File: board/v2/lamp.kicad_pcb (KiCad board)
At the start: 4 copper layers, 28 x 28 mm, 41 parts, among them J1 Conn_01x01_Female, J2 Conn_01x01_Female, J3 Conn_01x01_Female, J4 Conn_01x01_Female, J5 Conn_01x01_Female, J6 Conn_01x01_Female, J7 Conn_01x01_Female, J8 Conn_ARM_JTAG_SWD_10, U1 STM32G071GxU, U2 TLV2333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

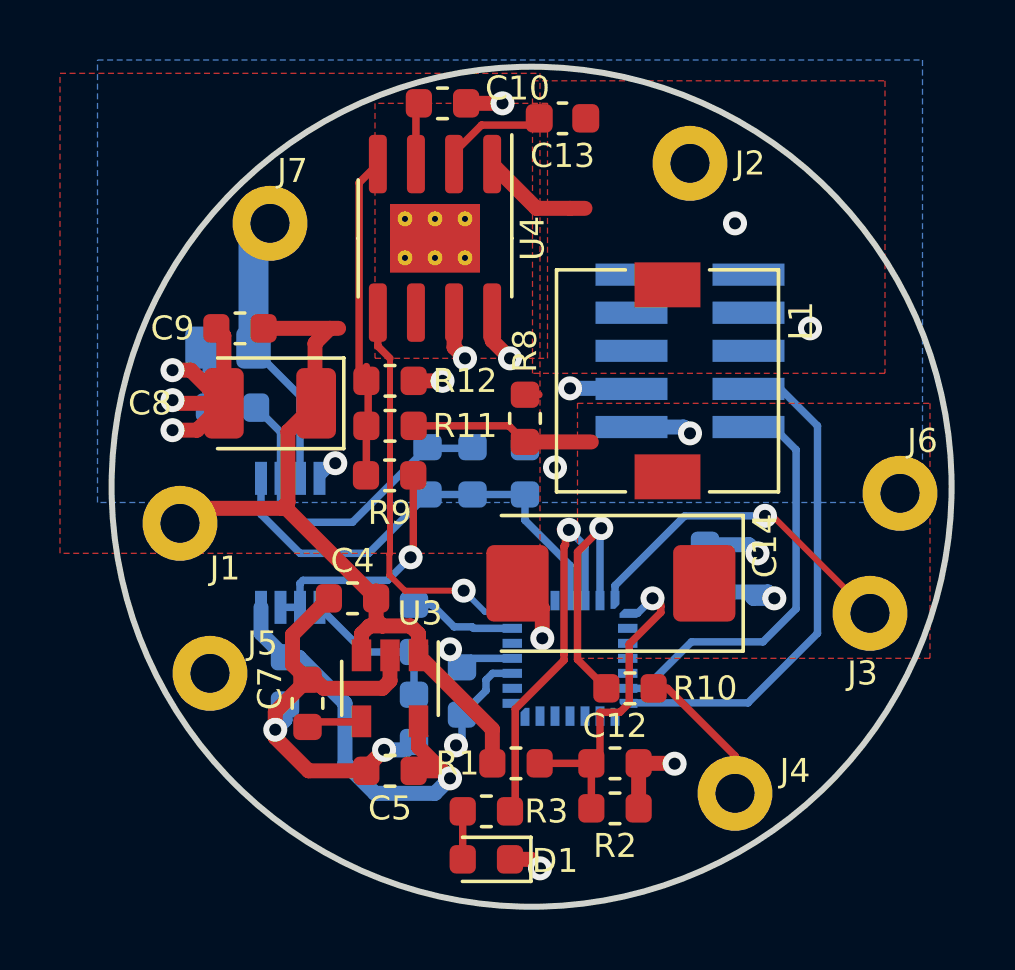
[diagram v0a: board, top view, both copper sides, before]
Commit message: hardware: Add reverse polarity protection
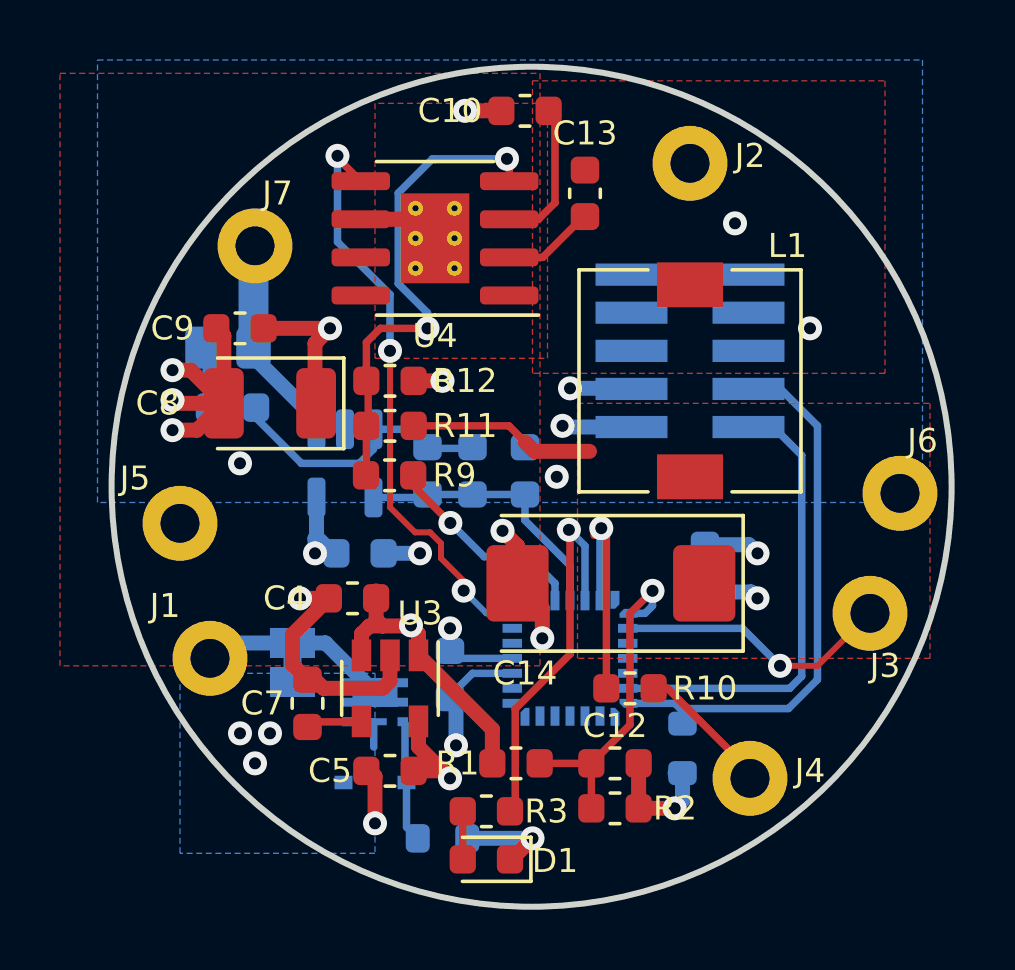
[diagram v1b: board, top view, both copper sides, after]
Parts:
- removed C3: 100n, Capacitor_SMD:C_0603_1608Metric
- removed R8: 100k, Resistor_SMD:R_0603_1608Metric
- added D2: D_Zener, Diode_SMD:D_SOD-323, B.Cu at (130.5, 93.6)
- added JP1: Jumper_2_Bridged, Jumper:SolderJumper-2_P1.3mm_Bridged_Pad1.0x1.5mm, B.Cu at (127.8, 89.6)
- added Q1: SiA453EDJ, Package_TO_SOT_SMD:Vishay_PowerPAK_SC70-6L_Single, B.Cu at (130.5, 91.0)
- added R7: R, Resistor_SMD:R_0603_1608Metric, B.Cu at (132.8, 95.5)
- R1: value 47k -> 680k
- R11: value 8.2k -> 100k
- R12: value 2.2k -> 47k
- R2, R9: value 10k -> 220k
- R4: value 10k -> 470k
- U2: value TLV2333 -> TLV333; footprint Package_SO:TSSOP-8_3x3mm_P0.65mm -> Package_TO_SOT_SMD:SOT-23-5
- moved R4 9.80 mm to (140.8, 92.5)
- moved J5 5.10 mm to (124.0, 85.0)
- moved C11 4.93 mm to (130.0, 86.0), turned to 0 degrees
- moved J1 4.61 mm to (125.0, 89.5)
- moved U2 3.22 mm to (129.5, 83.0)
- moved C10 2.76 mm to (135.5, 71.2), turned to 180 degrees
- moved C13 2.61 mm to (137.5, 74.0), turned to 90 degrees
- moved J7 0.90 mm to (126.5, 75.8)
- moved L1 0.75 mm to (141.0, 80.2)
- moved J4 0.71 mm to (143.0, 93.5)
- moved C2 0.68 mm to (133.0, 90.0)
- turned U4 to 180 degrees
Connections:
- C4 pad 1: /VIN -> /Vin
- C8 pad 1: /VIN -> /Vin
- C9 pad 1: /VIN -> /Vin
- J1 pad 1: /VIN -> /Vbat
- R1 pad 2: /VIN -> /Vin
- R4 pad 1: /SETPOINT -> GND
- R4 pad 2: /SETPOINT_PWM -> /SWDCLK
- R9 pad 2: Net-(R9-Pad2) -> /SETPOINT
- U1 pad 10: unconnected-(U1-Pad10) -> /SETPOINT
- U1 pad 14: /BTN -> unconnected-(U1-Pad14)
- U1 pad 16: unconnected-(U1-Pad16) -> /BTN
- U1 pad 6: /SETPOINT_PWM -> unconnected-(U1-Pad6)
- U2 pad 1: /ISENSE_BUFD -> /ISENSE
- U2 pad 2: Net-(C6-Pad1) -> GND
- U2 pad 3: /ISENSE -> Net-(C6-Pad1)
- U2 pad 4: GND -> /ISENSE_BUFD
- U2 pad 5: /SETPOINT -> +3V3
- U3 pad 1: /VIN -> /Vin
- U3 pad 3: /VIN -> /Vin
- U4 pad 6: unconnected-(U4-Pad6) -> GND
- U4 pad 7: /VIN -> /Vin
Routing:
- net /VIN: track 27.4 -> 0.00 mm, vias 1 -> 0
- net /Vin: track 0.00 -> 15.4 mm, vias 0 -> 6
- net Net-(R9-Pad2): track 8.27 -> 0.00 mm, vias 1 -> 0
- net +3V3: track 22.8 -> 16.0 mm, vias 4 -> 5
- net /ISENSE_BUFD: track 15.5 -> 9.11 mm
- net /Vbat: track 0.00 -> 6.40 mm
- net /EN: track 13.5 -> 19.5 mm, vias 1 -> 3
- net Net-(R11-Pad2): track 11.2 -> 16.9 mm, vias 0 -> 2
- net Net-(Q1-Pad3): track 0.00 -> 4.09 mm
- net /SW: track 3.71 -> 0.00 mm
- net /SETPOINT_PWM: track 3.60 -> 0.00 mm
- net Net-(C10-Pad1): track 2.07 -> 4.91 mm
- net /ISENSE: track 8.54 -> 6.56 mm
- net /BTN: track 11.3 -> 9.32 mm
- net Net-(C6-Pad1): track 11.2 -> 9.24 mm
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- added copper zone on B.Cu, net /Vin
- added copper zone on F.Cu, net /Vin
- added copper zone on In2.Cu, net /Vin
- removed copper zone on F.Cu, net /VIN
- removed copper zone on In2.Cu, net /VIN
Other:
- board text added: "BAT"
- board text removed: "VIN"

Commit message: hardware: More fiddling
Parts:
- moved C9 1.00 mm to (125.0, 78.5)
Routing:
- net /Vin: track 15.4 -> 13.0 mm
- net GND: track 44.1 -> 43.0 mm
- net /Vbat: track 6.40 -> 5.67 mm

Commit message: hardware: More wibbles
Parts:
- removed the C1 at (141.5, 86.5)
- D1: value LED -> GREEN
- D2: value D_Zener -> 5.1V; footprint Diode_SMD:D_SOD-323 -> Diode_SMD:D_SOD-123
- JP1: footprint Jumper:SolderJumper-2_P1.3mm_Bridged_Pad1.0x1.5mm -> Jumper:SolderJumper-2_P1.3mm_Bridged_RoundedPad1.0x1.5mm
- Q1: value SiA453EDJ -> SIA483DJ-T1-GE3‎
- moved R7 1.68 mm to (134.2, 94.8)
- moved D2 0.44 mm to (130.2, 94.0)
- renumbered C2 to C1
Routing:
- net GND: track 43.0 -> 40.0 mm, vias 18 -> 17
- net +3V3: track 15.9 -> 13.9 mm, vias 5 -> 4
- net Net-(D2-Pad2): track 4.02 -> 4.92 mm
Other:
- rule pad_to_mask_clearance: 0.2 -> 0
- board text added: "LED driver @bgamari Rev. ${REVISION}"

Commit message: board changes
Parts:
- JP1: footprint Jumper:SolderJumper-2_P1.3mm_Bridged_RoundedPad1.0x1.5mm -> Jumper:SolderJumper-2_P1.3mm_Open_RoundedPad1.0x1.5mm
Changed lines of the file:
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@@
     (property "Sheetname" "")
     (attr smd)
-    (fp_text reference "C7" (at 0 -1.5 unlocked) (layer "F.SilkS")
+    (fp_text reference "C7" (at -0.5 -1.5 unlocked) (layer "F.SilkS")
       (effects (font (size 0.8 0.8) (thickness 0.12)))
     )
@@
     )
   )
-  (footprint "Jumper:SolderJumper-2_P1.3mm_Bridged_RoundedPad1.0x1.5mm" (layer "B.Cu")
+  (footprint "Jumper:SolderJumper-2_P1.3mm_Open_RoundedPad1.0x1.5mm" (layer "B.Cu")
     (at 127.75 89.6375 -90)
-    (descr "SMD Solder Jumper, 1x1.5mm, rounded Pads, 0.3mm gap, bridged with 1 copper strip")
+    (descr "SMD Solder Jumper, 1x1.5mm, rounded Pads, 0.3mm gap, open")
     (tags "solder jumper open")
     (property "Sheetfile" "lamp.kicad_sch")
     (property "Sheetname" "")
     (attr exclude_from_pos_files)
-    (fp_text reference "JP1" (at -1.8875 0 unlocked) (layer "B.SilkS")
-      (effects (font (size 0.8 0.8) (thickness 0.12)) (justify mirror))
+    (fp_text reference "JP1" (at -2.1375 0 180) (layer "B.SilkS")
+      (effects (font (size 0.8 0.8) (thickness 0.15)) (justify mirror))
     )
     (fp_text value "Jumper_2_Bridged" (at 0 -1.9 90) (layer "B.Fab")
       (effects (font (size 1 1) (thickness 0.15)) (justify mirror))
     )
-    (fp_poly (pts (xy 0.25 0.3)
-      (xy -0.25 0.3)
-      (xy -0.25 -0.3)
-      (xy 0.25 -0.3)) (layer "B.Cu") (width 0) (fill solid))
+    (fp_line (start -1.4 -0.3) (end -1.4 0.3) (layer "B.SilkS") (width 0.12))
     (fp_line (start 1.4 0.3) (end 1.4 -0.3) (layer "B.SilkS") (width 0.12))
+    (fp_line (start -0.7 1) (end 0.7 1) (layer "B.SilkS") (width 0.12))
     (fp_line (start 0.7 -1) (end -0.7 -1) (layer "B.SilkS") (width 0.12))
-    (fp_line (start -0.7 1) (end 0.7 1) (layer "B.SilkS") (width 0.12))
-    (fp_line (start -1.4 -0.3) (end -1.4 0.3) (layer "B.SilkS") (width 0.12))
+    (fp_arc (start -0.7 -0.3) (end -1.4 -0.3) (angle 90) (layer "B.SilkS") (width 0.12))
+    (fp_arc (start 0.7 0.3) (end 1.4 0.3) (angle 90) (layer "B.SilkS") (width 0.12))
+    (fp_arc (start -0.7 0.3) (end -0.7 1) (angle 90) (layer "B.SilkS") (width 0.12))
     (fp_arc (start 0.7 -0.3) (end 0.7 -1) (angle 90) (layer "B.SilkS") (width 0.12))
-    (fp_arc (start 0.7 0.3) (end 1.4 0.3) (angle 90) (layer "B.SilkS") (width 0.12))
-    (fp_arc (start -0.7 -0.3) (end -1.4 -0.3) (angle 90) (layer "B.SilkS") (width 0.12))
-    (fp_arc (start -0.7 0.3) (end -0.7 1) (angle 90) (layer "B.SilkS") (width 0.12))
-    (fp_line (start 1.65 -1.25) (end 1.65 1.25) (layer "B.CrtYd") (width 0.05))
     (fp_line (start 1.65 -1.25) (end -1.65 -1.25) (layer "B.CrtYd") (width 0.05))
     (fp_line (start -1.65 1.25) (end -1.65 -1.25) (layer "B.CrtYd") (width 0.05))
     (fp_line (start -1.65 1.25) (end 1.65 1.25) (layer "B.CrtYd") (width 0.05))
+    (fp_line (start 1.65 -1.25) (end 1.65 1.25) (layer "B.CrtYd") (width 0.05))
     (pad "1" smd custom locked (at -0.65 0 270) (size 1 0.5) (layers "B.Cu" "B.Mask")
       (net 44 "/Vbat") (pinfunction "A") (pintype "passive") (zone_connect 2)

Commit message: board: Update kicad
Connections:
- net /~RESET renamed /~{RESET}
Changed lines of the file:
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@@
-(kicad_pcb (version 20210424) (generator pcbnew)
+(kicad_pcb (version 20210623) (generator pcbnew)
   (general
     (thickness 4.48)
@@
   (net 14 "Net-(J4-Pad1)")
   (net 15 "Net-(C7-Pad1)")
-  (net 16 "/~RESET")
+  (net 16 "/~{RESET}")
   (net 17 "unconnected-(J8-Pad8)")
   (net 18 "Net-(C10-Pad1)")
@@
       (net 3 "GND") (pinfunction "GNDDetect") (pintype "passive"))
     (pad "10" smd rect locked (at 1.95 -2.54) (size 2.4 0.74) (layers "B.Cu" "B.Paste" "B.Mask")
-      (net 16 "/~RESET") (pinfunction "~RESET~") (pintype "open_collector"))
+      (net 16 "/~{RESET}") (pinfunction "~RESET~") (pintype "open_collector"))
     (model "${KISYS3DMOD}/Connector_PinHeader_1.27mm.3dshapes/PinHeader_2x05_P1.27mm_Vertical_SMD.wrl"
       (offset (xyz 0 0 0))

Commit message: board: Hardware fixes from assembly
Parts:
- C10: value 4.7n -> 2.2u
- C13: value 10n -> 2.2u
- D2: value 5.1V -> 15V
- JP1: value Jumper_2_Bridged -> Jumper_2_Open
- R7: value R -> 100
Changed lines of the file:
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@@
       (net 3 "GND") (pinfunction "GND") (pintype "power_in"))
     (pad "3" smd rect locked (at -1.1 0.95 270) (size 1.06 0.65) (layers "F.Cu" "F.Paste" "F.Mask")
-      (net 43 "/Vin") (pinfunction "ON/~OFF~") (pintype "input"))
+      (net 43 "/Vin") (pinfunction "ON/~{OFF}") (pintype "input"))
     (pad "4" smd rect locked (at 1.1 0.95 270) (size 1.06 0.65) (layers "F.Cu" "F.Paste" "F.Mask")
       (net 15 "Net-(C7-Pad1)") (pinfunction "BP") (pintype "input"))
@@
       (effects (font (size 0.8 0.8) (thickness 0.12)))
     )
-    (fp_text value "4.7n" (at 0 1.43) (layer "F.Fab")
+    (fp_text value "2.2u" (at 0 1.43) (layer "F.Fab")
       (effects (font (size 1 1) (thickness 0.15)))
     )
@@
       (effects (font (size 0.8 0.8) (thickness 0.12)))
     )
-    (fp_text value "10n" (at 0 1.43 90) (layer "F.Fab")
+    (fp_text value "2.2u" (at 0 1.43 90) (layer "F.Fab")
       (effects (font (size 1 1) (thickness 0.15)))
     )
@@
       (effects (font (size 0.8 0.8) (thickness 0.12)) (justify mirror))
     )
-    (fp_text value "R" (at 0 -1.43) (layer "B.Fab")
+    (fp_text value "100" (at 0 -1.43) (layer "B.Fab")
       (effects (font (size 1 1) (thickness 0.15)) (justify mirror))
     )
@@
       (net 3 "GND") (pinfunction "VSS/VSSA") (pintype "power_in"))
     (pad "5" smd rect locked (at -1.925 -0.5 270) (size 0.3 0.65) (layers "B.Cu" "B.Paste" "B.Mask")
-      (net 21 "/RESET") (pinfunction "~RST~/PF2") (pintype "bidirectional"))
+      (net 21 "/RESET") (pinfunction "~{RST}/PF2") (pintype "bidirectional"))
     (pad "6" smd rect locked (at -1.925 -1 270) (size 0.3 0.65) (layers "B.Cu" "B.Paste" "B.Mask")
       (net 25 "unconnected-(U1-Pad6)") (pinfunction "PA0") (pintype "bidirectional+no_connect"))
@@
       (effects (font (size 0.8 0.8) (thickness 0.12)) (justify mirror))
     )
-    (fp_text value "5.1V" (at 0 -2.1 180) (layer "B.Fab")
+    (fp_text value "15V" (at 0 -2.1 180) (layer "B.Fab")
       (effects (font (size 1 1) (thickness 0.15)) (justify mirror))
     )
@@
       (effects (font (size 0.8 0.8) (thickness 0.15)) (justify mirror))
     )
-    (fp_text value "Jumper_2_Bridged" (at 0 -1.9 90) (layer "B.Fab")
+    (fp_text value "Jumper_2_Open" (at 0 -1.9 90) (layer "B.Fab")
       (effects (font (size 1 1) (thickness 0.15)) (justify mirror))
     )
@@
       (net 3 "GND") (pinfunction "GNDDetect") (pintype "passive"))
     (pad "10" smd rect locked (at 1.95 -2.54) (size 2.4 0.74) (layers "B.Cu" "B.Paste" "B.Mask")
-      (net 16 "/~{RESET}") (pinfunction "~RESET~") (pintype "open_collector"))
+      (net 16 "/~{RESET}") (pinfunction "~{RESET}") (pintype "open_collector"))
     (model "${KISYS3DMOD}/Connector_PinHeader_1.27mm.3dshapes/PinHeader_2x05_P1.27mm_Vertical_SMD.wrl"
       (offset (xyz 0 0 0))
